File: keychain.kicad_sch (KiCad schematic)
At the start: 2 parts, among them U1 ST25DV04K-JFR6D3

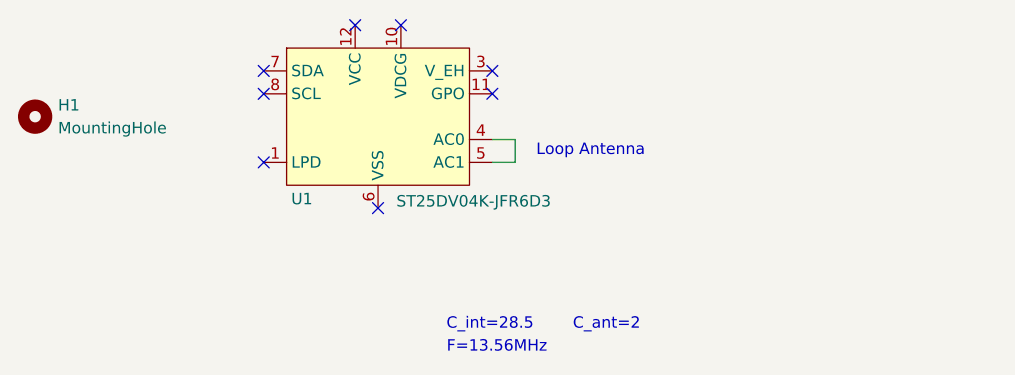
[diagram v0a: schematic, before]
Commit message: Add antenna inductance calculations
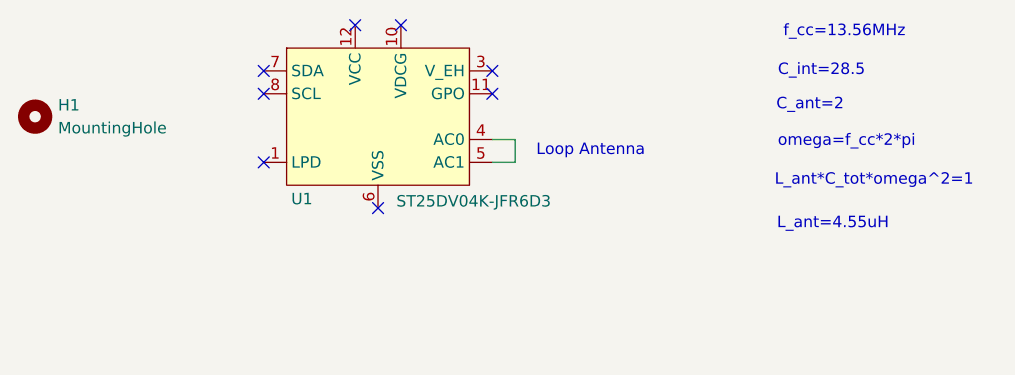
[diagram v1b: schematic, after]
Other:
- note added: "L_ant*C_tot*omega^2=1"
- note added: "L_ant=4.55uH"
- note added: "f_cc=13.56MHz"
- note added: "omega=f_cc*2*pi"
- note removed: "F=13.56MHz"
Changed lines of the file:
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@@
 	(text "C_int=28.5"
 		(exclude_from_sim no)
-		(at 101.346 86.614 0)
+		(at 138.176 58.42 0)
 		(effects
 			(font
@@
 		)
 	)
-	(text "F=13.56MHz"
+	(text "f_cc=13.56MHz"
 		(exclude_from_sim no)
-		(at 102.108 89.154 0)
+		(at 140.716 54.102 0)
+		(effects
+			(font
+				(size 1.27 1.27)
+			)
+		)
+	)
+	(text "L_ant=4.55uH"
+		(exclude_from_sim no)
+		(at 139.446 75.438 0)
 		(effects
 			(font
@@
 	(text "C_ant=2"
 		(exclude_from_sim no)
-		(at 114.3 86.614 0)
+		(at 136.906 62.23 0)
 		(effects
 			(font
+				(size 1.27 1.27)
+			)
+		)
+	)
+	(text "omega=f_cc*2*pi"
+		(exclude_from_sim no)
+		(at 140.97 66.294 0)
+		(effects
+			(font
+				(size 1.27 1.27)
+			)
+		)
+	)
+	(text "L_ant*C_tot*omega^2=1"
+		(exclude_from_sim no)
+		(at 144.018 70.612 0)
+		(effects
+			(font
